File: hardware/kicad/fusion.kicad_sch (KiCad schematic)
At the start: 32 parts, among them J1 BATTERY, J2 LSM6DSOX, J3 PICKIT, J4 HC-05, J5 FLEX, J7 FTDI, SW1 BUTTON, SW2 POWER, SW3 UART, U1 MCP1603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

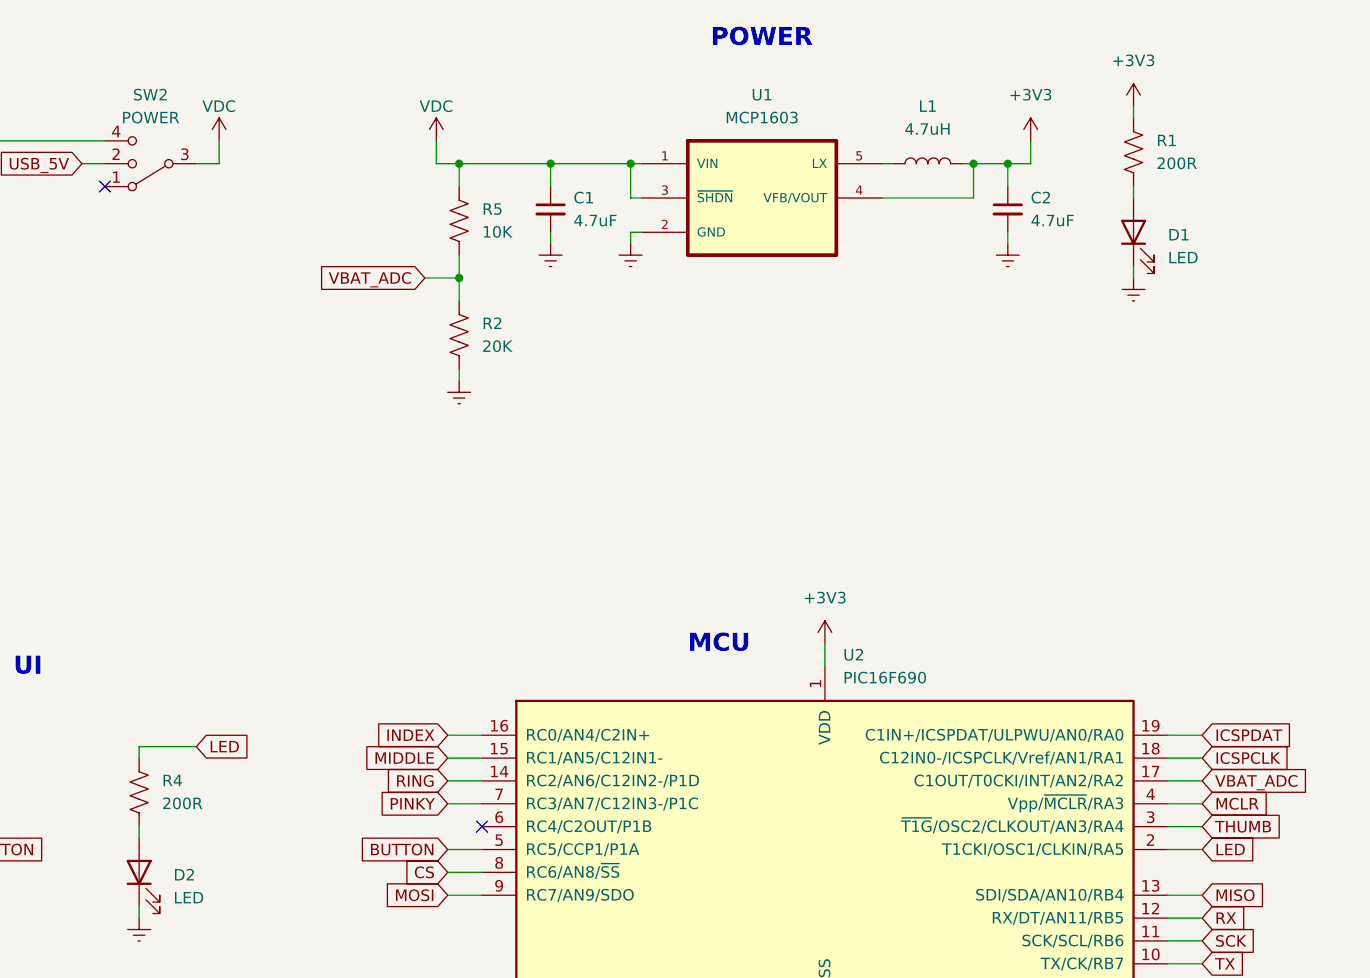
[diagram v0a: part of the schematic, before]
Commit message: Switch LED resistors to 220R as per DigiKey availability
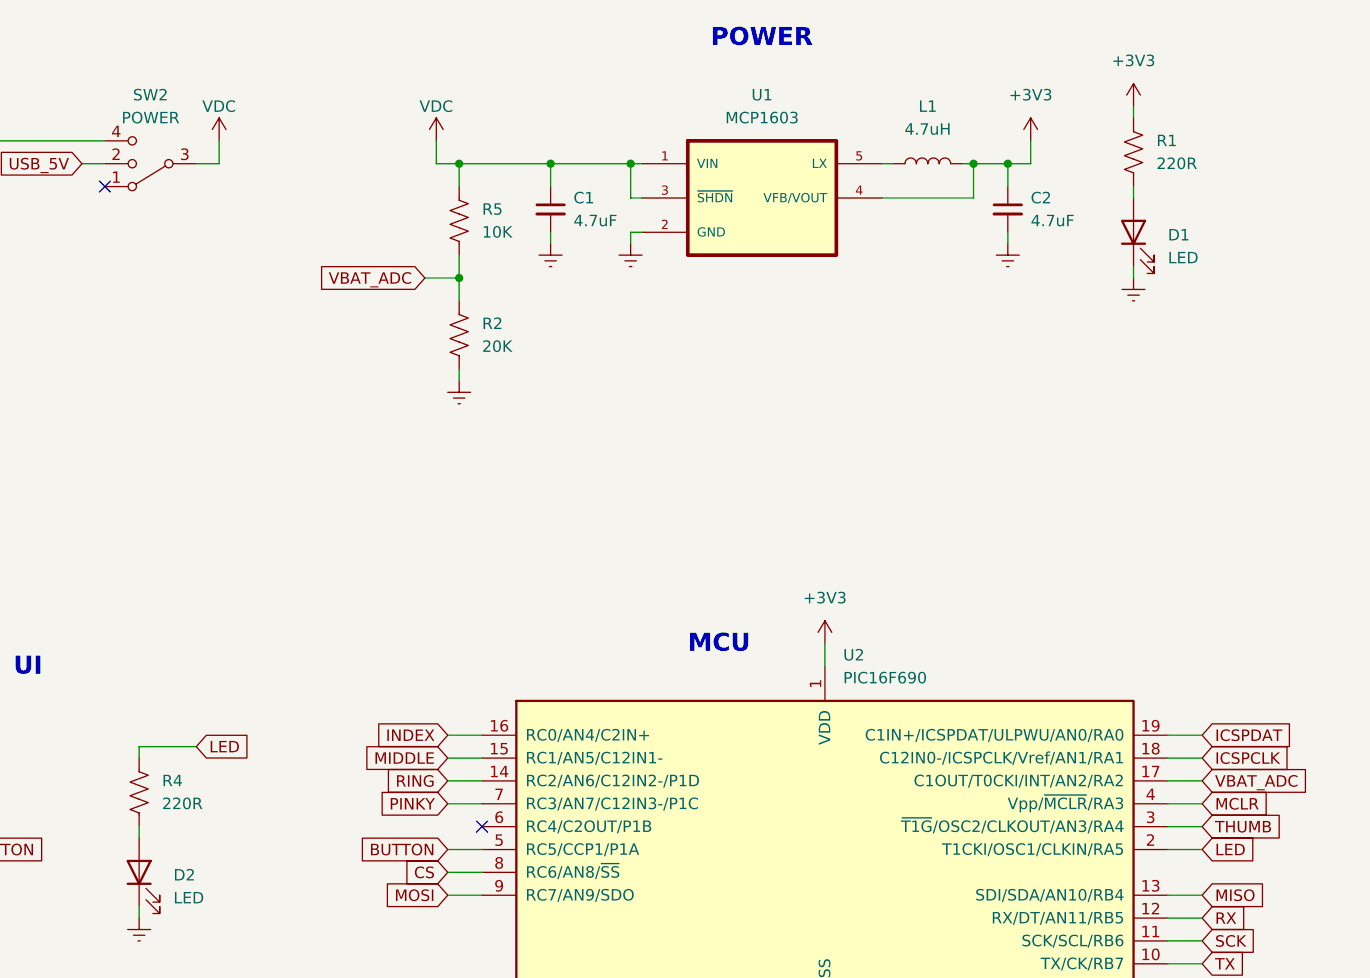
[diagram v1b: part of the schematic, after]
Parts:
- R1, R4: value 200R -> 220R
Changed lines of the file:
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@@
       (effects (font (size 1.27 1.27)) (justify right))
     )
-    (property "Value" "200R" (id 1) (at 171.45 38.0999 0)
+    (property "Value" "220R" (id 1) (at 171.45 38.0999 0)
       (effects (font (size 1.27 1.27)) (justify right))
     )
@@
       (effects (font (size 1.27 1.27)) (justify right))
     )
-    (property "Value" "200R" (id 1) (at 60.96 109.2199 0)
+    (property "Value" "220R" (id 1) (at 60.96 109.2199 0)
       (effects (font (size 1.27 1.27)) (justify right))
     )
@@
     )
     (path "/aa11bcd6-4a41-4882-8d8b-423f845f7cd1"
-      (reference "R1") (unit 1) (value "200R") (footprint "Resistor_SMD:R_0603_1608Metric_Pad0.98x0.95mm_HandSolder")
+      (reference "R1") (unit 1) (value "220R") (footprint "Resistor_SMD:R_0603_1608Metric_Pad0.98x0.95mm_HandSolder")
     )
     (path "/1f601946-0139-4682-8421-7cd20232376e"
@@
     )
     (path "/fdd90794-8a70-4f1e-8ba2-a31b07d0ddc1"
-      (reference "R4") (unit 1) (value "200R") (footprint "Resistor_SMD:R_0603_1608Metric_Pad0.98x0.95mm_HandSolder")
+      (reference "R4") (unit 1) (value "220R") (footprint "Resistor_SMD:R_0603_1608Metric_Pad0.98x0.95mm_HandSolder")
     )
     (path "/7fc32e22-3110-4b46-8606-afcca554e179"
